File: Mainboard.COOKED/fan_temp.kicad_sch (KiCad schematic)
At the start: 23 parts, among them M1 Fan_4pin, M2 Fan_4pin

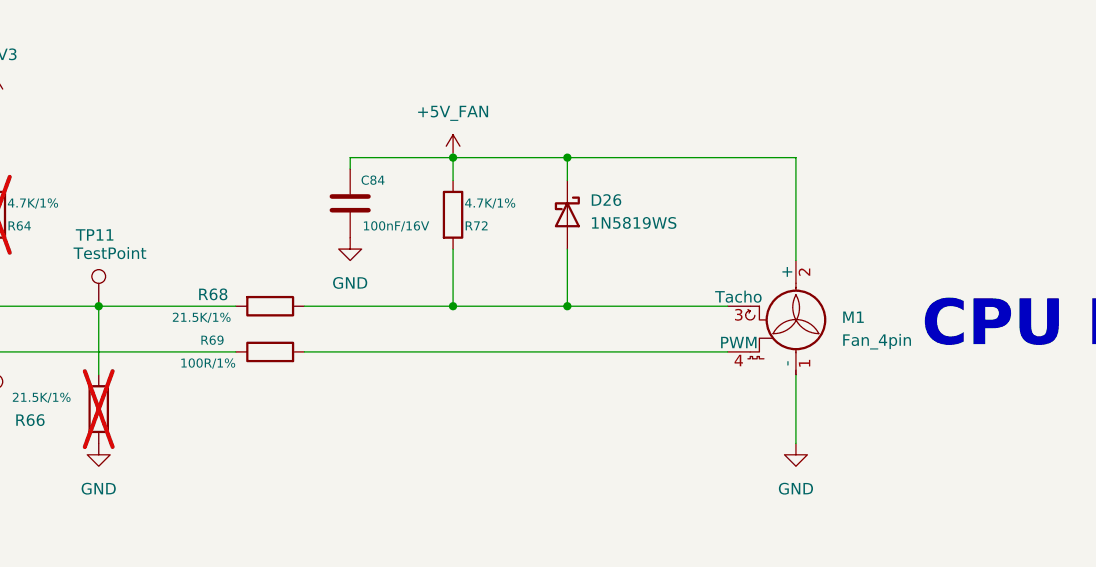
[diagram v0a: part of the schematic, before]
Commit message: "Scrapped" the current Mainboard, seems to be very broken for no reason.
It is being kept for now so that work done for the displays can be copied over later.
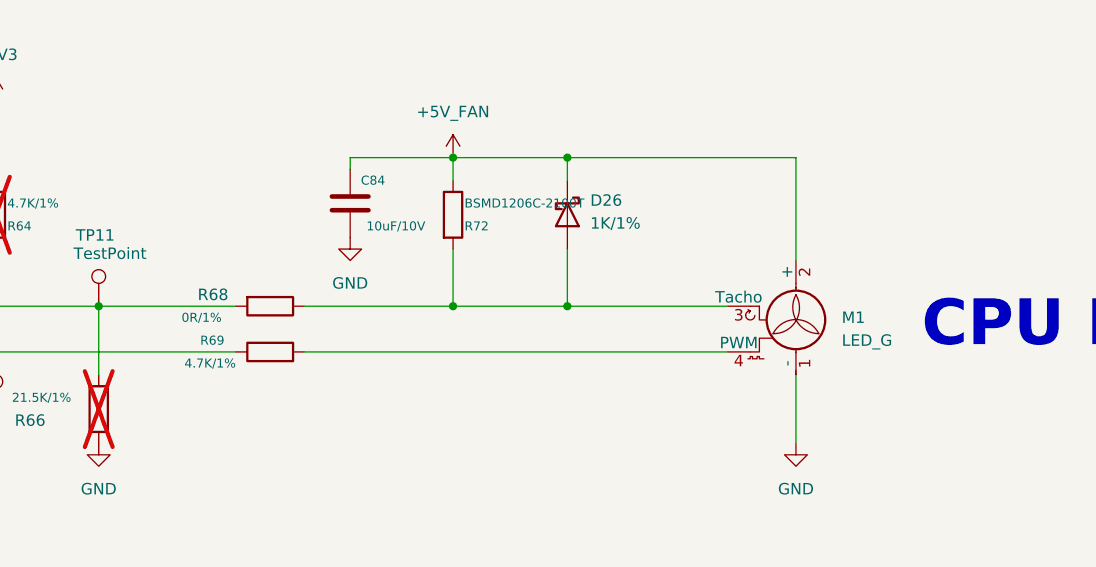
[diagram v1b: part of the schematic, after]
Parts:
- C84: value 100nF/16V -> 10uF/10V; DF_Comment 贴片电容0402-100nF-16V-X7R(0402) -> 贴片电容0402-10UF-10V-X5R_GRM155R61A106ME44D; SCH_Show_Footprint C0402 -> -- mixed values --
- D26: value 1N5819WS -> 1K/1%; footprint A_DFRobot:D_SOD-323 -> A_HDJ_Library:R_0402_1005Metric; DF_Comment 二极管-1N5819W-SOD323备选型号:B5819WS、JSPD140A -> 贴片电阻0402-1K-1%; SCH_Show_Footprint SOD-323 -> (none)
- M1: value Fan_4pin -> LED_G; footprint A_HDJ_Library:JST_PH_B4B-PH-K_1x04_P2.00mm_Vertical -> A_HDJ_Library:LED_0603_1608Metric; Buy_Link https://item.szlcsc.com/255571.html -> (none); DF_Comment PH2.0-4A直针插座(2.0-4P直)-DL -> 贴片LED蓝色0603(0603); SCH_Show_Footprint (none) -> LED0603
- R68: value 21.5K/1% -> 0R/1%; footprint A_DFRobot:R_0402 -> A_HDJ_Library:R_0402_1005Metric; DF_Comment 贴片电阻0402-21.5K-1% -> 贴片电阻0402-0R-1%
- R69: value 100R/1% -> 4.7K/1%; footprint A_DFRobot:R_0402 -> A_HDJ_Library:R_0402_1005Metric; DF_Comment 贴片电阻0402-100R-1% -> 贴片电阻0402-4.7K-1%
- R72: value 4.7K/1% -> BSMD1206C-2100T; footprint A_DFRobot:R_0402 -> Resistor_SMD:R_1206_3216Metric; Buy_Link (none) -> https://item.szlcsc.com/43118985.html; DF_Comment 贴片电阻0402-4.7K-1% -> 一次性保险丝_BSMD1206C-2100T_32V-10A
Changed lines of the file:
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@@
 			)
 		)
-		(property "Value" "100R/1%"
+		(property "Value" "4.7K/1%"
 			(at 328.93 168.91 90)
 			(show_name no)
@@
 			)
 		)
-		(property "Footprint" "A_DFRobot:R_0402"
+		(property "Footprint" "A_HDJ_Library:R_0402_1005Metric"
 			(at 332.74 169.418 90)
 			(hide yes)
@@
 			)
 		)
-		(property "DF_Comment" "贴片电阻0402-100R-1%"
+		(property "DF_Comment" "贴片电阻0402-4.7K-1%"
 			(at 332.74 167.64 0)
 			(hide yes)
@@
 			)
 		)
-		(property "Value" "100nF/16V"
+		(property "Value" "10uF/10V"
 			(at 346.71 153.67 0)
 			(show_name no)
@@
 			)
 		)
-		(property "DF_Comment" "贴片电容0402-100nF-16V-X7R(0402)"
+		(property "DF_Comment" "贴片电容0402-10UF-10V-X5R_GRM155R61A106ME44D"
 			(at 341.63 151.13 0)
 			(hide yes)
@@
 			)
 		)
-		(property "SCH_Show_Footprint" "C0402"
+		(property "SCH_Show_Footprint" "-- mixed values --"
 			(at 341.63 151.13 0)
 			(hide yes)
@@
 			)
 		)
-		(property "Value" "Fan_4pin"
+		(property "Value" "LED_G"
 			(at 396.24 166.37 0)
 			(show_name no)
@@
 			)
 		)
-		(property "Footprint" "A_HDJ_Library:JST_PH_B4B-PH-K_1x04_P2.00mm_Vertical"
+		(property "Footprint" "A_HDJ_Library:LED_0603_1608Metric"
 			(at 391.16 164.846 0)
 			(hide yes)
@@
 			)
 		)
-		(property "Datasheet" "http://www.formfactors.org/developer%5Cspecs%5Crev1_2_public.pdf"
+		(property "Datasheet" ""
 			(at 391.16 164.846 0)
 			(hide yes)
@@
 			)
 		)
-		(property "Buy_Link" "https://item.szlcsc.com/255571.html"
+		(property "Buy_Link" ""
 			(at 391.16 165.1 0)
 			(hide yes)
@@
 			)
 		)
-		(property "DF_Comment" "PH2.0-4A直针插座(2.0-4P直)-DL"
+		(property "DF_Comment" "贴片LED蓝色0603(0603)"
 			(at 391.16 165.1 0)
 			(hide yes)
@@
 			)
 		)
-		(property "SCH_Show_Footprint" ""
+		(property "SCH_Show_Footprint" "LED0603"
 			(at 391.16 165.1 0)
 			(hide yes)
@@
 			)
 		)
-		(property "Value" "21.5K/1%"
+		(property "Value" "0R/1%"
 			(at 325.12 163.83 90)
 			(show_name no)
@@
 			)
 		)
-		(property "Footprint" "A_DFRobot:R_0402"
+		(property "Footprint" "A_HDJ_Library:R_0402_1005Metric"
 			(at 332.74 160.782 90)
 			(hide yes)
@@
 			)
 		)
-		(property "DF_Comment" "贴片电阻0402-21.5K-1%"
+		(property "DF_Comment" "贴片电阻0402-0R-1%"
 			(at 332.74 162.56 0)
 			(hide yes)
@@
 			)
 		)
-		(property "Value" "1N5819WS"
+		(property "Value" "1K/1%"
 			(at 368.3 153.3525 90)
 			(show_name no)
@@
 			)
 		)
-		(property "Footprint" "A_DFRobot:D_SOD-323"
+		(property "Footprint" "A_HDJ_Library:R_0402_1005Metric"
 			(at 361.315 152.4 0)
 			(hide yes)
@@
 			)
 		)
-		(property "Datasheet" "https://datasheet.lcsc.com/lcsc/2204281430_Guangdong-Hottech-1N5819WS_C191023.pdf"
+		(property "Datasheet" ""
 			(at 365.76 152.4 0)
 			(hide yes)
@@
 			)
 		)
-		(property "DF_Comment" "二极管-1N5819W-SOD323备选型号:B5819WS、JSPD140A"
+		(property "DF_Comment" "贴片电阻0402-1K-1%"
 			(at 365.76 152.4 0)
 			(hide yes)
@@
 			)
 		)
-		(property "SCH_Show_Footprint" "SOD-323"
+		(property "SCH_Show_Footprint" ""
 			(at 365.76 152.4 0)
 			(hide yes)
@@
 			)
 		)
-		(property "Value" "4.7K/1%"
+		(property "Value" "BSMD1206C-2100T"
 			(at 354.33 151.13 0)
 			(show_name no)
@@
 			)
 		)
-		(property "Footprint" "A_DFRobot:R_0402"
+		(property "Footprint" "Resistor_SMD:R_1206_3216Metric"
 			(at 351.282 152.4 90)
 			(hide yes)
@@
 			)
 		)
-		(property "Description" ""
+		(property "Description" "32V/10A"
 			(at 353.06 152.4 0)
 			(hide yes)
@@
 			)
 		)
-		(property "Buy_Link" ""
+		(property "Buy_Link" "https://item.szlcsc.com/43118985.html"
 			(at 353.06 152.4 0)
 			(hide yes)
@@
 			)
 		)
-		(property "DF_Comment" "贴片电阻0402-4.7K-1%"
+		(property "DF_Comment" "一次性保险丝_BSMD1206C-2100T_32V-10A"
 			(at 353.06 152.4 0)
 			(hide yes)
